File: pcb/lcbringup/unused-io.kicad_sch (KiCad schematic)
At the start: 1 part, among them U1 XC7A35T-2FGG484C

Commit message: Continued lcbringup layout
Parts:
- removed unit 6 of U1
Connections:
- no-connect marks 185 -> 135

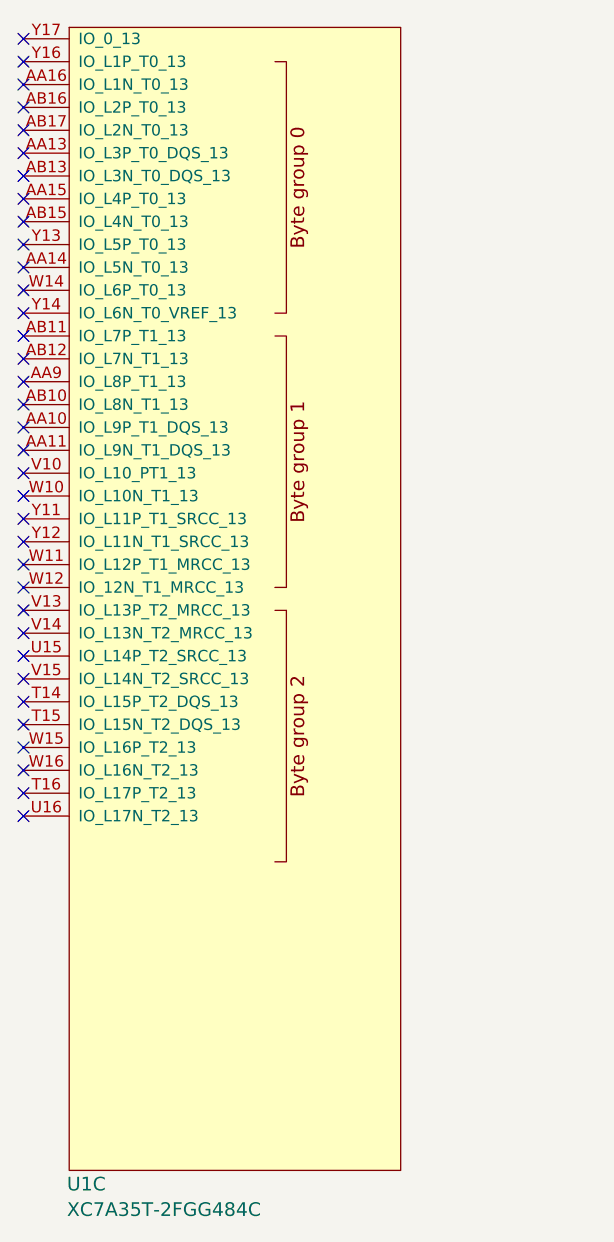
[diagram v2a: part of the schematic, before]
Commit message: Conitnued lcbringup layout, power supply is now floorplanned
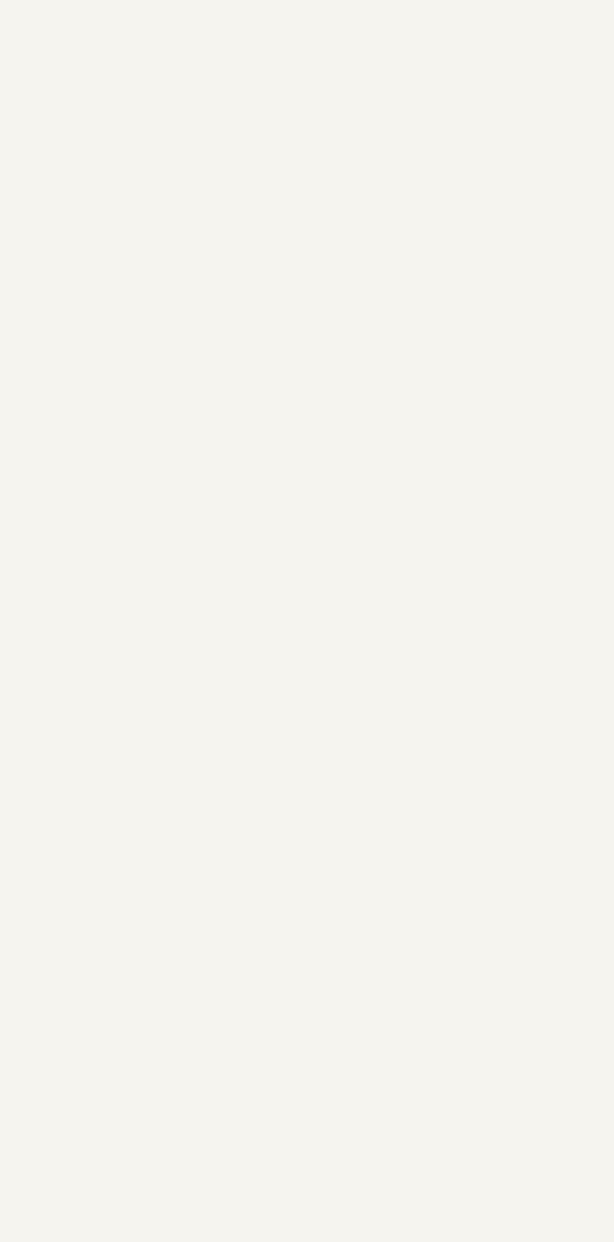
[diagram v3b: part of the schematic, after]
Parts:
- removed unit 3 of U1
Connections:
- no-connect marks 135 -> 100
